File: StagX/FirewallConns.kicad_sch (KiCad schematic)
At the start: 2 parts

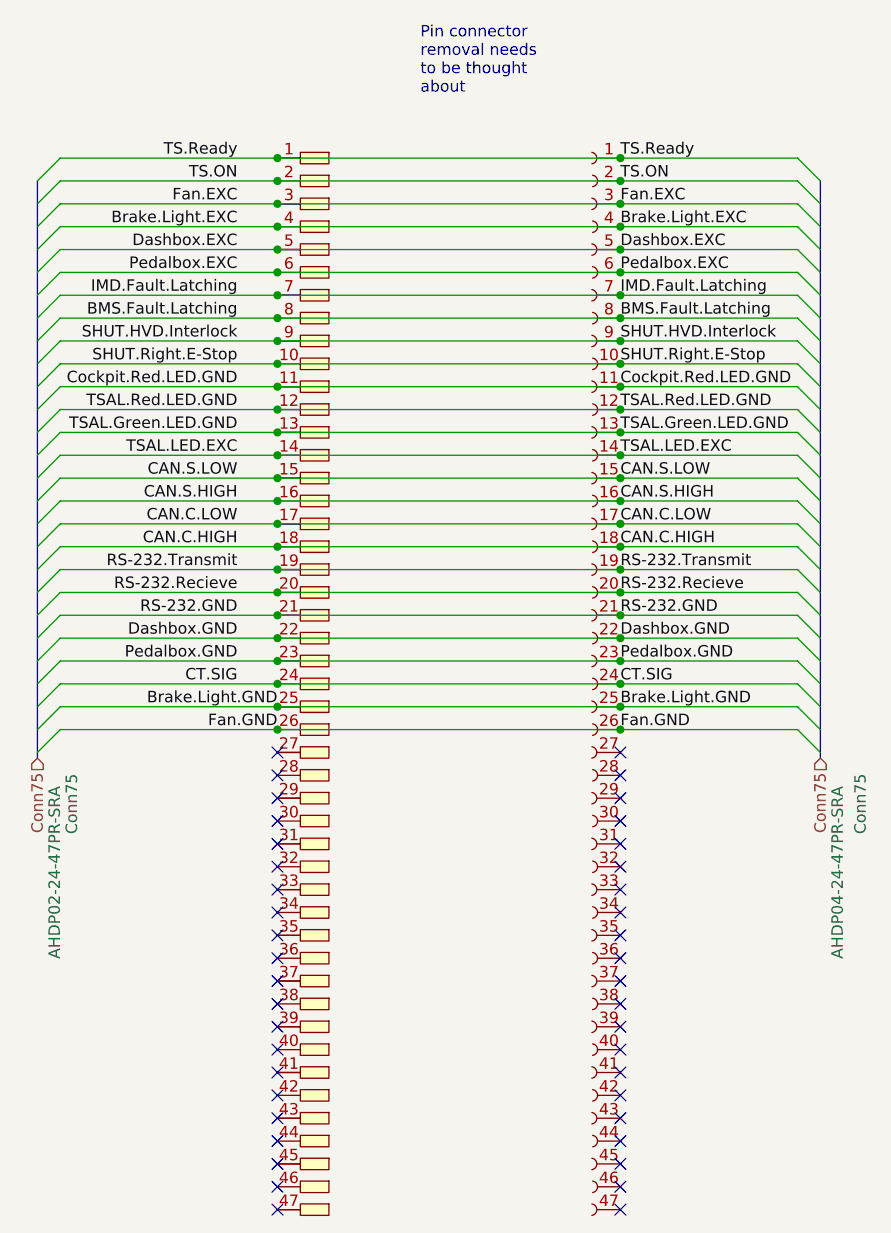
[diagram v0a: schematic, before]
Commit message: feat(FrontLoom): Completed front loom
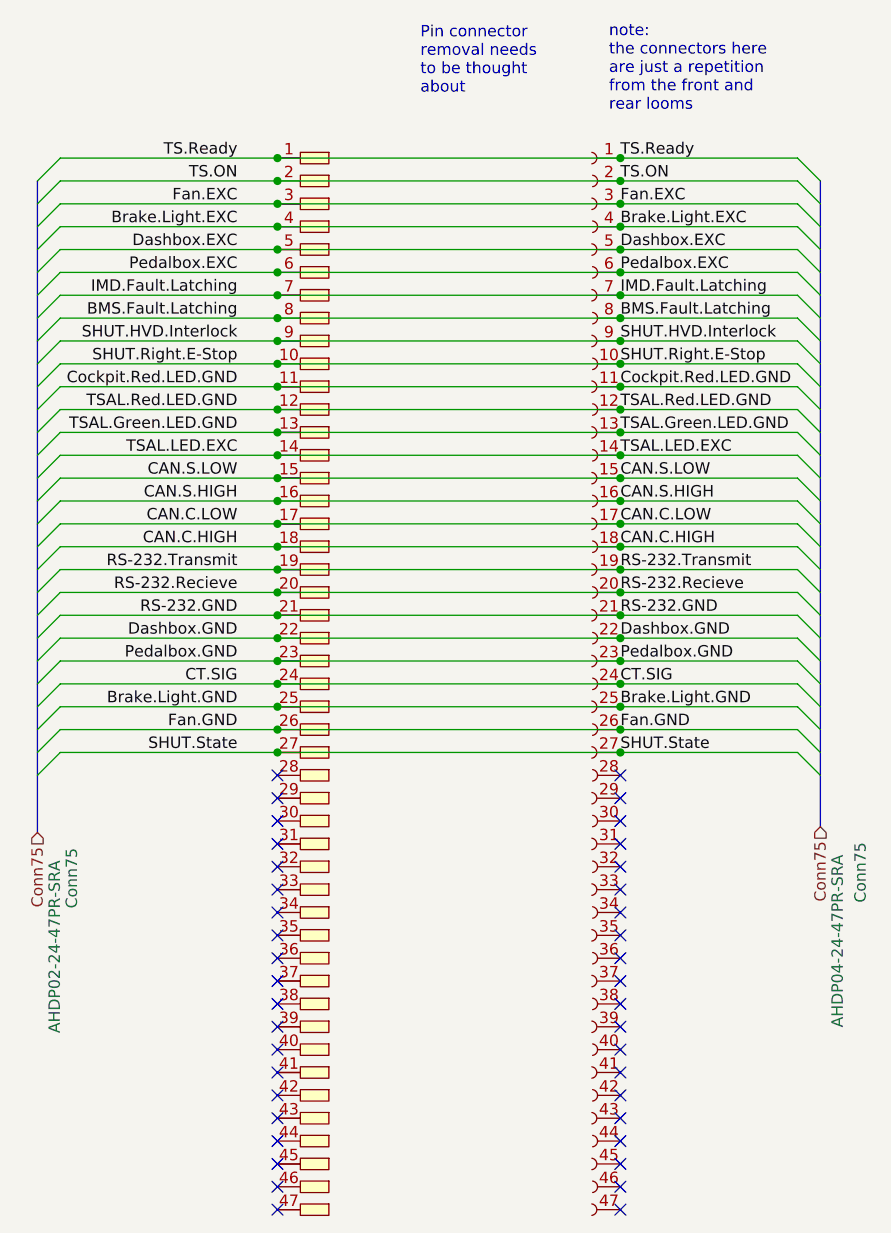
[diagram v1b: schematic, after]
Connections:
- net SHUT.State: now reaches Conn75.27
- net SHUT.State: now also Conn75.27
- no-connect marks 42 -> 40
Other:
- note added: "note: the connectors here are just a repetition from the front and rear looms"

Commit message: fix(FrontLoom): post review changes made
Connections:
- net Brake.Light.EXC: no longer names the net of Conn75.4, Conn75.4
- net Brake.Light.GND: no longer names the net of Conn75.25, Conn75.25
- net Fan.EXC renamed BPS.Rear.SIG
- net Fan.GND: no longer names the net of Conn75.26, Conn75.26
- net SHUT.State: no longer names the net of Conn75.27
- net SHUT.State: no longer Conn75.27
- no-connect marks 40 -> 42
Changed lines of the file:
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@@
     (title "Firewall")
     (date "2024-02-11")
-    (rev "1.0.0")
+    (rev "1.1.0")
     (company "SUFST")
     (comment 1 "Stag X")
@@
   (junction (at 76.2 107.95) (diameter 0) (color 0 0 0 0)
   )
-  (junction (at 76.2 110.49) (diameter 0) (color 0 0 0 0)
-  )
   (junction (at 114.3 72.39) (diameter 0) (color 0 0 0 0)
   )
@@
   )
   (junction (at 76.2 69.85) (diameter 0) (color 0 0 0 0)
-  )
-  (junction (at 114.3 110.49) (diameter 0) (color 0 0 0 0)
   )
   (junction (at 114.3 97.79) (diameter 0) (color 0 0 0 0)
@@
   (no_connect (at 76.2 161.29))
   (no_connect (at 114.3 113.03))
+  (no_connect (at 114.3 110.49))
   (no_connect (at 76.2 148.59))
   (no_connect (at 114.3 161.29))
@@
   (no_connect (at 76.2 138.43))
   (no_connect (at 76.2 130.81))
+  (no_connect (at 76.2 110.49))
   (no_connect (at 114.3 140.97))
   (no_connect (at 114.3 148.59))
@@
     (stroke (width 0) (type default))
   )
-  (bus_entry (at 52.07 110.49) (size -2.54 2.54)
-    (stroke (width 0) (type default))
-  )
   (bus_entry (at 133.985 102.87) (size 2.54 2.54)
     (stroke (width 0) (type default))
@@
     (stroke (width 0) (type default))
   )
-  (bus_entry (at 133.985 110.49) (size 2.54 2.54)
-    (stroke (width 0) (type default))
-  )
   (bus_entry (at 52.07 95.25) (size -2.54 2.54)
     (stroke (width 0) (type default))
@@
     (stroke (width 0) (type default))
   )
-  (bus (pts (xy 136.525 113.03) (xy 136.525 118.745))
+  (bus (pts (xy 136.525 110.49) (xy 136.525 118.745))
     (stroke (width 0) (type default))
   )
@@
     (stroke (width 0) (type default))
   )
-  (wire (pts (xy 114.3 110.49) (xy 133.985 110.49))
-    (stroke (width 0) (type default))
-  )
   (wire (pts (xy 52.07 46.99) (xy 76.2 46.99))
     (stroke (width 0) (type default))
@@
     (stroke (width 0) (type default))
   )
-  (wire (pts (xy 114.3 110.49) (xy 76.2 110.49))
-    (stroke (width 0) (type default))
-  )
   (bus (pts (xy 136.525 57.15) (xy 136.525 59.69))
     (stroke (width 0) (type default))
@@
     (stroke (width 0) (type default))
   )
-  (bus (pts (xy 49.53 110.49) (xy 49.53 113.03))
+  (bus (pts (xy 49.53 110.49) (xy 49.53 119.38))
     (stroke (width 0) (type default))
   )
@@
     (stroke (width 0) (type default))
   )
-  (bus (pts (xy 49.53 113.03) (xy 49.53 119.38))
-    (stroke (width 0) (type default))
-  )
   (wire (pts (xy 133.985 107.95) (xy 114.3 107.95))
     (stroke (width 0) (type default))
@@
     (stroke (width 0) (type default))
   )
-  (wire (pts (xy 76.2 110.49) (xy 52.07 110.49))
-    (stroke (width 0) (type default))
-  )
   (wire (pts (xy 76.2 92.71) (xy 114.3 92.71))
     (stroke (width 0) (type default))
@@
   )
   (bus (pts (xy 136.525 90.17) (xy 136.525 92.71))
-    (stroke (width 0) (type default))
-  )
-  (bus (pts (xy 136.525 110.49) (xy 136.525 113.03))
     (stroke (width 0) (type default))
   )
@@
     (effects (font (size 1.27 1.27)) (justify left bottom))
   )
-  (label "Fan.EXC" (at 71.755 49.53 180) (fields_autoplaced)
-    (effects (font (size 1.27 1.27)) (justify right bottom))
-  )
   (label "Pedalbox.EXC" (at 114.3 57.15 0) (fields_autoplaced)
     (effects (font (size 1.27 1.27)) (justify left bottom))
@@
     (effects (font (size 1.27 1.27)) (justify right bottom))
   )
-  (label "Brake.Light.GND" (at 71.755 105.41 180) (fields_autoplaced)
-    (effects (font (size 1.27 1.27)) (justify right bottom))
-  )
   (label "TSAL.Red.LED.GND" (at 114.3 72.39 0) (fields_autoplaced)
     (effects (font (size 1.27 1.27)) (justify left bottom))
@@
     (effects (font (size 1.27 1.27)) (justify left bottom))
   )
-  (label "Fan.GND" (at 114.3 107.95 0) (fields_autoplaced)
-    (effects (font (size 1.27 1.27)) (justify left bottom))
-  )
   (label "SHUT.HVD.Interlock" (at 114.3 64.77 0) (fields_autoplaced)
     (effects (font (size 1.27 1.27)) (justify left bottom))
@@
     (effects (font (size 1.27 1.27)) (justify left bottom))
   )
-  (label "Brake.Light.EXC" (at 71.755 52.07 180) (fields_autoplaced)
-    (effects (font (size 1.27 1.27)) (justify right bottom))
-  )
   (label "TSAL.Green.LED.GND" (at 114.3 74.93 0) (fields_autoplaced)
     (effects (font (size 1.27 1.27)) (justify left bottom))
@@
     (effects (font (size 1.27 1.27)) (justify right bottom))
   )
+  (label "BPS.Rear.SIG" (at 114.3 49.53 0) (fields_autoplaced)
+    (effects (font (size 1.27 1.27)) (justify left bottom))
+  )
   (label "BMS.Fault.Latching" (at 71.755 62.23 180) (fields_autoplaced)
     (effects (font (size 1.27 1.27)) (justify right bottom))
@@
     (effects (font (size 1.27 1.27)) (justify right bottom))
   )
-  (label "Brake.Light.EXC" (at 114.3 52.07 0) (fields_autoplaced)
-    (effects (font (size 1.27 1.27)) (justify left bottom))
-  )
   (label "CAN.C.HIGH" (at 114.3 87.63 0) (fields_autoplaced)
     (effects (font (size 1.27 1.27)) (justify left bottom))
   )
-  (label "SHUT.State" (at 114.3 110.49 0) (fields_autoplaced)
-    (effects (font (size 1.27 1.27)) (justify left bottom))
-  )
-  (label "Fan.EXC" (at 114.3 49.53 0) (fields_autoplaced)
-    (effects (font (size 1.27 1.27)) (justify left bottom))
-  )
   (label "SHUT.Right.E-Stop" (at 71.755 67.31 180) (fields_autoplaced)
     (effects (font (size 1.27 1.27)) (justify right bottom))
@@
     (effects (font (size 1.27 1.27)) (justify right bottom))
   )
-  (label "SHUT.State" (at 71.755 110.49 180) (fields_autoplaced)
-    (effects (font (size 1.27 1.27)) (justify right bottom))
-  )
   (label "Dashbox.GND" (at 71.755 97.79 180) (fields_autoplaced)
     (effects (font (size 1.27 1.27)) (justify right bottom))
@@
     (effects (font (size 1.27 1.27)) (justify left bottom))
   )
-  (label "Fan.GND" (at 71.755 107.95 180) (fields_autoplaced)
-    (effects (font (size 1.27 1.27)) (justify right bottom))
-  )
   (label "TSAL.LED.EXC" (at 114.3 77.47 0) (fields_autoplaced)
     (effects (font (size 1.27 1.27)) (justify left bottom))
@@
     (effects (font (size 1.27 1.27)) (justify right bottom))
   )
-  (label "Brake.Light.GND" (at 114.3 105.41 0) (fields_autoplaced)
-    (effects (font (size 1.27 1.27)) (justify left bottom))
-  )
   (label "RS-232.Transmit" (at 114.3 90.17 0) (fields_autoplaced)
     (effects (font (size 1.27 1.27)) (justify left bottom))
@@
     (effects (font (size 1.27 1.27)) (justify left bottom))
   )
+  (label "BPS.Rear.SIG" (at 71.755 49.53 180) (fields_autoplaced)
+    (effects (font (size 1.27 1.27)) (justify right bottom))
+  )
   (hierarchical_label "Conn75" (shape input) (at 49.53 119.38 270) (fields_autoplaced)
